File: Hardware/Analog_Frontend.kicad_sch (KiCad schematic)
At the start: 0 parts

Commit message: Design Analog Frontend
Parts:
- added C25 (x10): 1u, symbol Device:C
- added C25 (x12): 30p, symbol Device:C
- added C25 (x17): 100n, symbol Device:C
- added C25 (x5): 10u, symbol Device:C
- added C25: 200p, symbol Device:C
- added D2 (x4): D_Schottky, symbol Device:D_Schottky
- added IC10, IC11, IC12, IC13: INA823DGKR, BQ51003YFPR:SOP65P490X110-8N, symbol INA823DGKR:INA823DGKR
- added IC14: REF35160QDBVR, BQ51003YFPR:SOT95P280X145-6N, symbol REF35160QDBVR:REF35160QDBVR
- added IC15: LM324LVIDYYR, BQ51003YFPR:SOP50P326X110-14N, symbol LM324LVIDYYR:LM324LVIDYYR
- added IC8: AD8067ARTZ-REEL7, Package_TO_SOT_SMD:SOT-23-5, symbol AD8067ARTZ-REEL7:AD8067ARTZ-REEL7
- added IC9: ADA4898-2YRDZ, BQ51003YFPR:SOIC127P600X175-9N, symbol ADA4898-2YRDZ:ADA4898-2YRDZ
- added R4 (x8): 300k, symbol Device:R
- added R4 (x4): 10k, symbol Device:R
- added R4 (x8): 600k, symbol Device:R
- added R4: 4R, symbol Device:R
- added R4 (x2): 82.5k, symbol Device:R
- added R4: 2k, symbol Device:R
- added R4 (x4): 24.9k, symbol Device:R
- added R4 (x2): 100R, symbol Device:R
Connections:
- new net: C25.1, IC11.2 (-IN), R4.1, R4.2
- new net: C25.1, IC12.3 (+IN), R4.1, R4.2
- new net: C25.1, IC10.2 (-IN), R4.1, R4.2
- new net: IC10.1 (RG_1), R4.2
- new net: C25.1, IC10.3 (+IN), R4.1, R4.2
- new net: IC10.8 (RG_2), R4.1
- new net: C25.1, D2.1 (K), IC15.12 (IN4+), R4.1
- new net: C25.1, IC12.2 (-IN), R4.1, R4.2
- new net: C25.1, D2.1 (K), IC15.10 (IN3+), R4.1
- new net: C25.1, IC13.3 (+IN), R4.1, R4.2
- new net: C25.1, D2.1 (K), IC15.5 (IN2+), R4.1
- new net: C25.1, IC13.2 (-IN), R4.1, R4.2
- new net: IC13.1 (RG_1), R4.2
- new net: IC13.8 (RG_2), R4.1
- new net: IC8.1 (VOUT), R4.1, R4.1, R4.2
- new net: IC9.3 (+IN1), R4.1, R4.2
- new net: IC8.4 (-IN), R4.2
- new net: IC11.8 (RG_2), R4.1
- new net: IC11.1 (RG_1), R4.2
- new net: IC12.1 (RG_1), R4.2
- new net: IC12.8 (RG_2), R4.1
- new net: IC9.6 (-IN2), IC9.7 (VOUT2), R4.2
- new net: C25.1, IC9.2 (-IN1), R4.1, R4.2
- new net: C25.1, IC14.5 (NR)
- new net: C25.1, IC11.3 (+IN), R4.1, R4.2
- new net: C25.2, IC8.3 (+IN), IC9.1 (VOUT1)
- new net: C25.1, D2.1 (K), IC15.3 (IN1+), R4.1
- new net +3.3VA: C25.1, C25.1, C25.1, C25.1, C25.1, C25.1, C25.1, C25.1, C25.1, C25.1, C25.1, IC10.7 (+VS), IC11.7 (+VS), IC12.7 (+VS), IC13.7 (+VS), IC14.3 (EN), IC14.4 (VIN), IC15.4 (V+)
- new net -3V3: C25.1, C25.1, C25.1, C25.1, C25.1, C25.1, C25.1, C25.1, IC10.4 (-VS), IC11.4 (-VS), IC12.4 (-VS), IC13.4 (-VS)
- new net GNDA: C25.2, C25.2, C25.2, C25.2, C25.2, C25.2, C25.2, C25.2, C25.2, C25.2, C25.2, C25.2, C25.2, C25.2, C25.2, C25.2, C25.2, C25.2, C25.2, C25.2, C25.2, C25.2, C25.2, C25.2, C25.2, C25.2, C25.2, C25.2, C25.2, C25.2, C25.2, C25.2, C25.2, C25.2, C25.2, C25.2, C25.2, C25.2, C25.2, C25.2, C25.2, C25.2, C25.2, C25.2, D2.2 (A), D2.2 (A), D2.2 (A), D2.2 (A), IC14.1 (GND_1), IC14.2 (GND_2), IC15.11 (V-), R4.1, R4.1, R4.1, R4.1, R4.1, R4.1, R4.1, R4.1
- new net P_1: IC15.1 (OUT1), IC15.2 (IN1-)
- new net P_2: IC15.6 (IN2-), IC15.7 (OUT2)
- new net P_3: IC15.8 (OUT3), IC15.9 (IN3-)
- new net P_4: IC15.13 (IN4-), IC15.14 (OUT4)
- new net Probe_1: IC10.6 (OUT), R4.2
- new net Probe_2: IC11.6 (OUT), R4.2
- new net Probe_3: IC12.6 (OUT), R4.2
- new net Probe_4: IC13.6 (OUT), R4.2
- new net Probe_in_1+: R4.2
- new net Probe_in_1-: R4.2
- new net Probe_in_2+: R4.2
- new net Probe_in_2-: R4.2
- new net Probe_in_3+: R4.2
- new net Probe_in_3-: R4.2
- new net Probe_in_4+: R4.2
- new net Probe_in_4-: R4.2
- new net Stim+: C25.1, C25.1, C25.1, C25.1, IC8.5 (+VS), IC9.8 (+VS)
- new net Stim-: C25.1, C25.1, C25.1, C25.1, IC8.2 (-VS), IC9.4 (-VS), IC9.9 (EP)
- new net Stim_control+: C25.1, C25.1, R4.1
- new net Stim_control-: R4.1
- new net Stim_out: IC9.5 (+IN2), R4.2
- new net Vref: C25.1, C25.1, IC10.5 (REF), IC11.5 (REF), IC12.5 (REF), IC13.5 (REF), IC14.6 (VREF)
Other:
- note added: "1.6V Reference"
- note added: "Composite Enhanced Howland Current Source"
- note added: "Negative Voltage Protection"
- note added: "Probe Input Amplifiers"

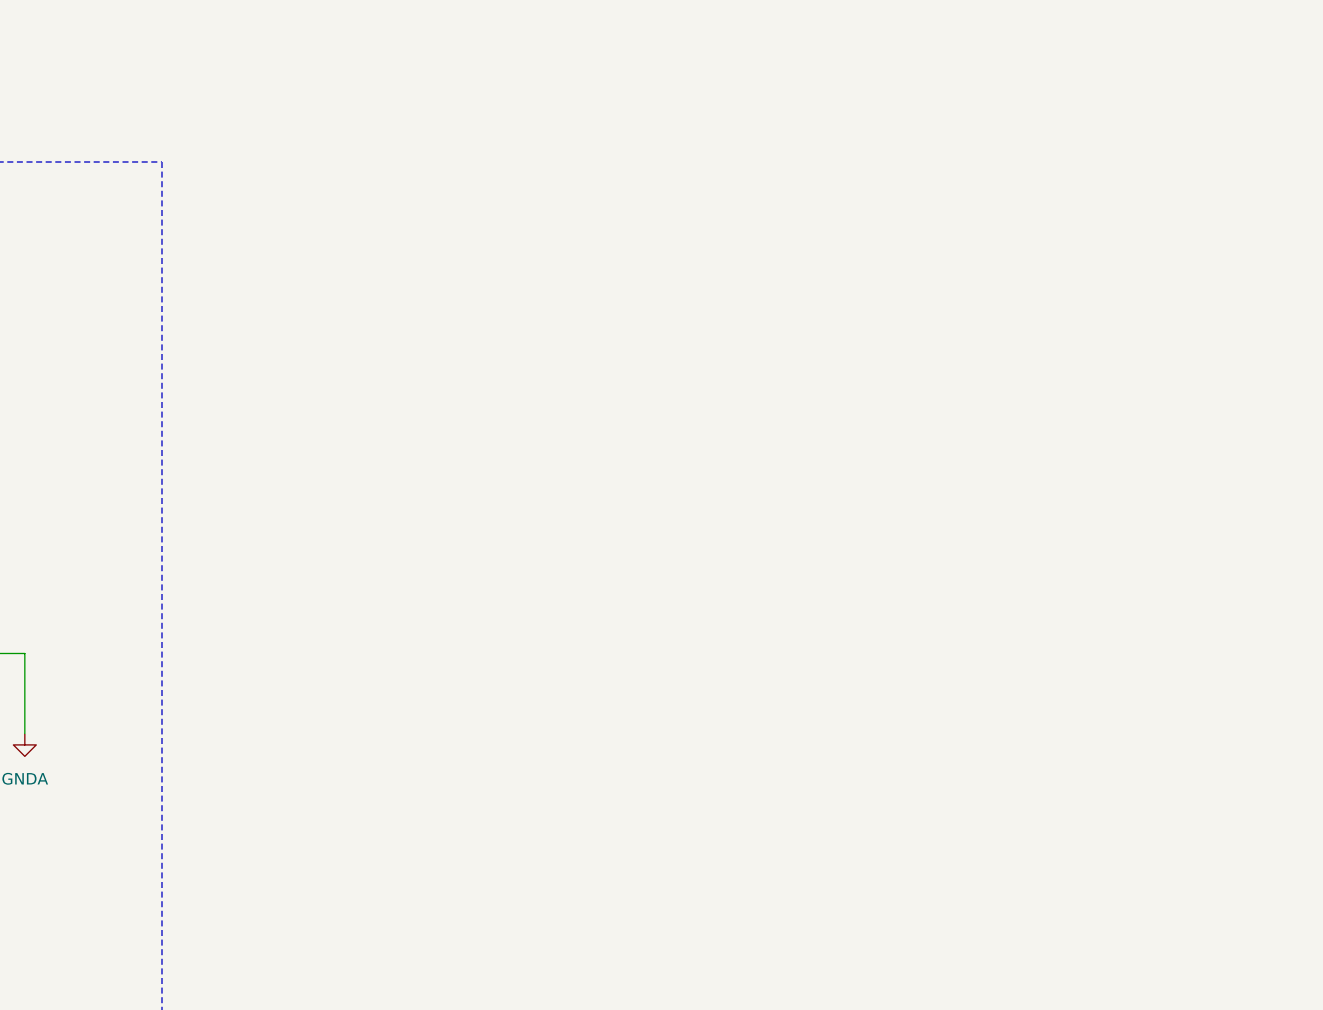
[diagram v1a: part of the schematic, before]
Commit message: Add Current Measurement
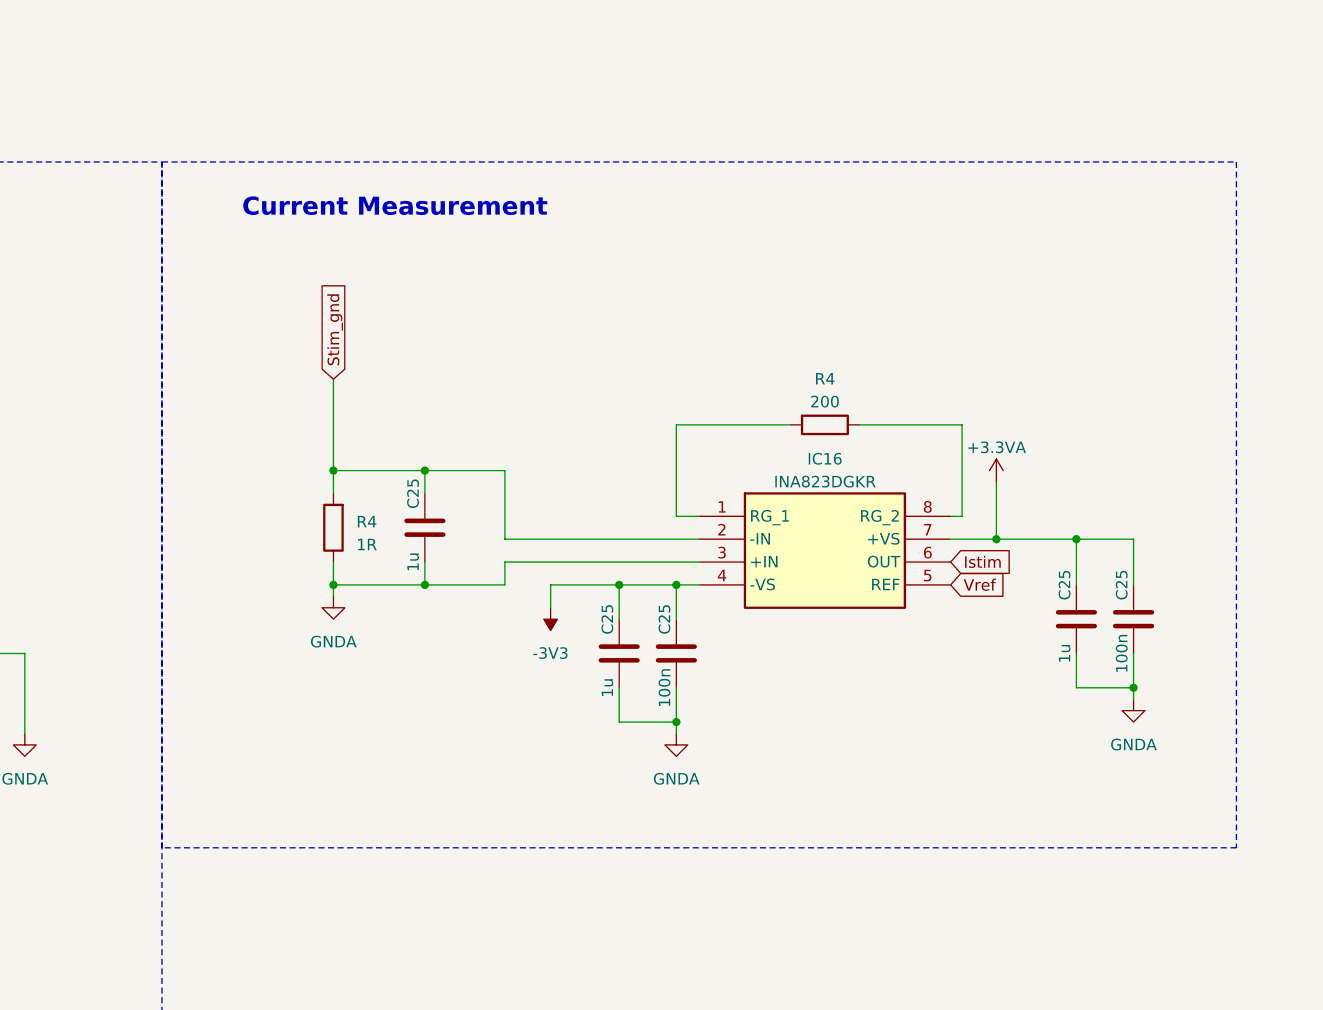
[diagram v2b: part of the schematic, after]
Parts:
- added C25 (x2): 100n, symbol Device:C
- added C25 (x3): 1u, symbol Device:C
- added IC16: INA823DGKR, BQ51003YFPR:SOP65P490X110-8N, symbol INA823DGKR:INA823DGKR
- added R4: 200, symbol Device:R
- added R4: 1R, symbol Device:R
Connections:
- net +3.3VA: now also C25.1, C25.1, IC16.7 (+VS)
- net -3V3: now also C25.1, C25.1, IC16.4 (-VS)
- net GNDA: now also C25.2, C25.2, C25.2, C25.2, C25.2, IC16.3 (+IN), R4.1
- net Vref: now also IC16.5 (REF)
- new net: IC16.8 (RG_2), R4.1
- new net: IC16.1 (RG_1), R4.2
- new net Istim: IC16.6 (OUT)
- new net Stim_gnd: C25.1, IC16.2 (-IN), R4.2
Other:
- note added: "Current Measurement"

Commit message: Spec all components
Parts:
- added C25: 1u, Capacitor_SMD:C_0603_1608Metric, symbol Device:C
- added J13: Conn_01x10, Connector_PinHeader_2.54mm:PinHeader_1x10_P2.54mm_Vertical, symbol Connector_Generic:Conn_01x10
- added J14: 505110-1092, BQ51003YFPR:5051101092, symbol 505110-1092:505110-1092
- added J2 (x5): Conn_01x02, Connector_PinHeader_2.54mm:PinHeader_1x02_P2.54mm_Vertical, symbol Connector_Generic:Conn_01x02
- C25: footprint (none) -> Capacitor_SMD:C_0603_1608Metric
- C25: footprint (none) -> Capacitor_SMD:C_0402_1005Metric
- C25: footprint (none) -> Capacitor_SMD:C_0805_2012Metric
- D2: value D_Schottky -> CDBU0130L-HF; footprint (none) -> Diode_SMD:D_0603_1608Metric
- R4: value 300k -> 332k; footprint (none) -> Resistor_SMD:R_0402_1005Metric
- R4: footprint (none) -> Resistor_SMD:R_0402_1005Metric
- R4: footprint (none) -> Resistor_SMD:R_0603_1608Metric
- renumbered IC12 to IC10, IC13 to IC11, IC14 to IC12, IC15 to IC13, IC9 to IC14, IC8 to IC15, IC10 to IC8, IC11 to IC9
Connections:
- net GNDA: now also J14.11, J14.12
- net Istim: now also J2.1 (Pin_1)
- net P_1: now also J2.1 (Pin_1)
- net P_2: now also J2.1 (Pin_1)
- net P_3: now also J2.1 (Pin_1)
- net P_4: now also J2.1 (Pin_1)
- net Probe_in_1+: now also J13.1 (Pin_1), J14.1
- net Probe_in_1-: now also J13.2 (Pin_2), J14.2
- net Probe_in_2+: now also J13.3 (Pin_3), J14.3
- net Probe_in_2-: now also J13.4 (Pin_4), J14.4
- net Probe_in_3+: now also J13.5 (Pin_5), J14.5
- net Probe_in_3-: now also J13.6 (Pin_6), J14.6
- net Probe_in_4+: now also J13.7 (Pin_7), J14.7
- net Probe_in_4-: now also J13.8 (Pin_8), J14.8
- net Stim_gnd: now also J13.10 (Pin_10), J14.10
- net Stim_out: now also C25.1, J13.9 (Pin_9), J14.9; no longer IC14.5 (+IN2), R4.2
- new net: C25.2, IC14.5 (+IN2), R4.2
- new net ADC_1: J2.2 (Pin_2)
- new net ADC_2: J2.2 (Pin_2)
- new net ADC_3: J2.2 (Pin_2)
- new net ADC_4: J2.2 (Pin_2)
- new net ADC_5: J2.2 (Pin_2)
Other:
- note added: "Probe Connector"
- moved on the sheet: C25, D2, IC13, IC14, IC15, IC16, R4

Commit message: Start Layout
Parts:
- removed C25 (x2): 100n, Capacitor_SMD:C_0402_1005Metric, symbol Device:C
- removed IC10, IC11, IC16, IC8, IC9: INA823DGKR, BQ51003YFPR:SOP65P490X110-8N, symbol INA823DGKR:INA823DGKR
- removed IC12: REF35160QDBVR, BQ51003YFPR:SOT95P280X145-6N, symbol REF35160QDBVR:REF35160QDBVR
- removed IC13: LM324LVIDYYR, BQ51003YFPR:SOP50P326X110-14N, symbol LM324LVIDYYR:LM324LVIDYYR
- removed IC14: ADA4898-2YRDZ, BQ51003YFPR:SOIC127P600X175-9N, symbol ADA4898-2YRDZ:ADA4898-2YRDZ
- removed IC15: AD8067ARTZ-REEL7, Package_TO_SOT_SMD:SOT-23-5, symbol AD8067ARTZ-REEL7:AD8067ARTZ-REEL7
- removed J14: 505110-1092, BQ51003YFPR:5051101092, symbol 505110-1092:505110-1092
- removed J2 (x4): Conn_01x02, Connector_PinHeader_2.54mm:PinHeader_1x02_P2.54mm_Vertical, symbol Connector_Generic:Conn_01x02
- added C25 (x2): 1u, Capacitor_SMD:C_0603_1608Metric, symbol Device:C
- added C25 (x3): 100n, Capacitor_SMD:C_0402_1005Metric, symbol Device:C
- added C25: 10u, Capacitor_SMD:C_0805_2012Metric, symbol Device:C
- added IC10, IC11, IC16, IC8, IC9: INA823DGKR, Neural_Footprints:SOP65P490X110-8N, symbol Neural_Components:INA823DGKR
- added IC12: REF35160QDBVR, Neural_Footprints:SOT95P280X145-6N, symbol Neural_Components:REF35160QDBVR
- added IC13: LM324LVIDYYR, Neural_Footprints:SOP50P326X110-14N, symbol Neural_Components:LM324LVIDYYR
- added IC14: ADA4898-2YRDZ, Neural_Footprints:SOIC127P600X175-9N, symbol Neural_Components:ADA4898-2YRDZ
- added IC15: AD8067ARTZ-REEL7, Neural_Footprints:SOT95P280X145-5N, symbol Neural_Components:AD8067ARTZ-REEL7
- added IC17: MCP3464RT-E_NC, Neural_Footprints:QFN40P300X300X60-21N-D, symbol Neural_Components:MCP3464RT-E_NC
- added J10 (x4): Conn_01x03, Connector_PinHeader_2.54mm:PinHeader_1x03_P2.54mm_Vertical, symbol Connector_Generic:Conn_01x03
- added J17: 505110-1092, Neural_Footprints:5051101092, symbol Neural_Components:505110-1092
- added R4 (x8): 10R, Resistor_SMD:R_0402_1005Metric, symbol Device:R
- renumbered J13 to J16
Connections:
- net +3.3VA: now also IC10.7 (+VS), IC11.7 (+VS), IC12.3 (EN), IC12.4 (VIN), IC13.4 (V+), IC16.7 (+VS), IC8.7 (+VS), IC9.7 (+VS), R4.2
- net -3V3: now also IC10.4 (-VS), IC11.4 (-VS), IC16.4 (-VS), IC8.4 (-VS), IC9.4 (-VS)
- net ADC_1: now also J10.3 (Pin_3)
- net ADC_2: now also J10.3 (Pin_3)
- net ADC_3: now also J10.3 (Pin_3)
- net ADC_4: now also J10.3 (Pin_3)
- net GNDA: now also C25.2, C25.2, C25.2, C25.2, IC12.1 (GND_1), IC12.2 (GND_2), IC13.11 (V-), IC16.3 (+IN), IC17.1 (REFIN-), IC17.20 (AGND), IC17.21 (EP), J17.11, J17.12
- net Istim: now also IC16.6 (OUT)
- net P_1: now also IC13.1 (OUT1), IC13.2 (IN1-), J10.2 (Pin_2)
- net P_2: now also IC13.6 (IN2-), IC13.7 (OUT2), J10.2 (Pin_2)
- net P_3: now also IC13.8 (OUT3), IC13.9 (IN3-), J10.2 (Pin_2)
- net P_4: now also IC13.13 (IN4-), IC13.14 (OUT4), J10.2 (Pin_2)
- net Probe_1: now also IC8.6 (OUT)
- net Probe_2: now also IC9.6 (OUT)
- net Probe_3: now also IC10.6 (OUT)
- net Probe_4: now also IC11.6 (OUT)
- net Probe_in_1+: now also J16.2 (Pin_2), J17.2; no longer J16.1 (Pin_1)
- net Probe_in_1-: now also J16.1 (Pin_1), J17.1; no longer J16.2 (Pin_2)
- net Probe_in_2+: now also J16.4 (Pin_4), J17.4; no longer J16.3 (Pin_3)
- net Probe_in_2-: now also J16.3 (Pin_3), J17.3; no longer J16.4 (Pin_4)
- net Probe_in_3+: now also J16.6 (Pin_6), J17.6; no longer J16.5 (Pin_5)
- net Probe_in_3-: now also J16.5 (Pin_5), J17.5; no longer J16.6 (Pin_6)
- net Probe_in_4+: now also J16.8 (Pin_8), J17.8; no longer J16.7 (Pin_7)
- net Probe_in_4-: now also J16.7 (Pin_7), J17.7; no longer J16.8 (Pin_8)
- net Stim+: now also IC14.8 (+VS), IC15.5 (+VS)
- net Stim-: now also IC14.4 (-VS), IC14.9 (EP), IC15.2 (-VS)
- net Stim_gnd: now also IC16.2 (-IN), J17.10
- net Stim_out: now also J17.9
- net Vref: now also C25.1, C25.1, IC10.5 (REF), IC11.5 (REF), IC12.6 (VREF), IC16.5 (REF), IC17.2 (REFIN+/OUT), IC8.5 (REF), IC9.5 (REF)
- net at C25.1, R4.1, R4.2: now also IC9.2 (-IN)
- net at C25.1, R4.1, R4.2: now also IC10.3 (+IN)
- net at C25.1, R4.1, R4.2: now also IC8.2 (-IN)
- net at R4.2: now also IC8.1 (RG_1)
- net at C25.1, R4.1, R4.2: now also IC8.3 (+IN)
- net at R4.1: now also IC8.8 (RG_2)
- net at C25.1, D2.1 (K), R4.1: now also IC13.12 (IN4+)
- net at C25.1, R4.1, R4.2: now also IC10.2 (-IN)
- net at C25.1, D2.1 (K), R4.1: now also IC13.10 (IN3+)
- net at C25.1, R4.1, R4.2: now also IC11.3 (+IN)
- net at C25.1, D2.1 (K), R4.1: now also IC13.5 (IN2+)
- net at C25.1, R4.1, R4.2: now also IC11.2 (-IN)
- net at R4.2: now also IC11.1 (RG_1)
- net at R4.1: now also IC11.8 (RG_2)
- net at R4.1, R4.1, R4.2: now also IC15.1 (VOUT)
- net at C25.2, R4.2: now also IC14.5 (+IN2)
- net at R4.1, R4.2: now also IC14.3 (+IN1)
- net at R4.1: now also IC16.8 (RG_2)
- net at R4.2: now also IC16.1 (RG_1)
- net at R4.2: now also IC15.4 (-IN)
- net at R4.1: now also IC9.8 (RG_2)
- net at R4.2: now also IC9.1 (RG_1)
- net at R4.2: now also IC10.1 (RG_1)
- net at R4.1: now also IC10.8 (RG_2)
- net at R4.2: now also IC14.6 (-IN2), IC14.7 (VOUT2)
- net at C25.1, R4.1, R4.2: now also IC14.2 (-IN1)
- net at C25.1: now also IC12.5 (NR)
- net at C25.1, R4.1, R4.2: now also IC9.3 (+IN)
- net at C25.2: now also IC14.1 (VOUT1), IC15.3 (+IN)
- net at C25.1, D2.1 (K), R4.1: now also IC13.3 (IN1+)
- new net: IC17.16 (MCLK), R4.2
- new net: C25.1, C25.1, IC17.18 (DVDD), R4.1
- new net: IC17.14 (SDO), R4.2
- new net: IC17.15 (~{IRQ}/MDAT), R4.2
- new net: IC17.11 (~{CS}), R4.2
- new net: IC17.12 (SCK), R4.2
- new net: IC17.13 (SDI), R4.2
- new net: C25.1, C25.1, IC17.19 (AVDD), R4.1
- new net +3.3V: R4.2
- new net GND: C25.2, C25.2, IC17.17 (DGND)
- new net MCLK: R4.1
- new net OADC_1: IC17.3 (CH0), J10.1 (Pin_1)
- new net OADC_2: IC17.4 (CH1), J10.1 (Pin_1)
- new net OADC_3: IC17.5 (CH2), J10.1 (Pin_1)
- new net OADC_4: IC17.6 (CH3), J10.1 (Pin_1)
- new net SCK: R4.1
- new net SDI: R4.1
- new net SDO: R4.1
- new net ~{CS}: R4.1
- new net ~{IRQ}: R4.1
- no-connect marks 0 -> 4
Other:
- note added: "ADC"
